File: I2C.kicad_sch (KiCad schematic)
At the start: 12 parts, among them U15 TCA9548AMRGER

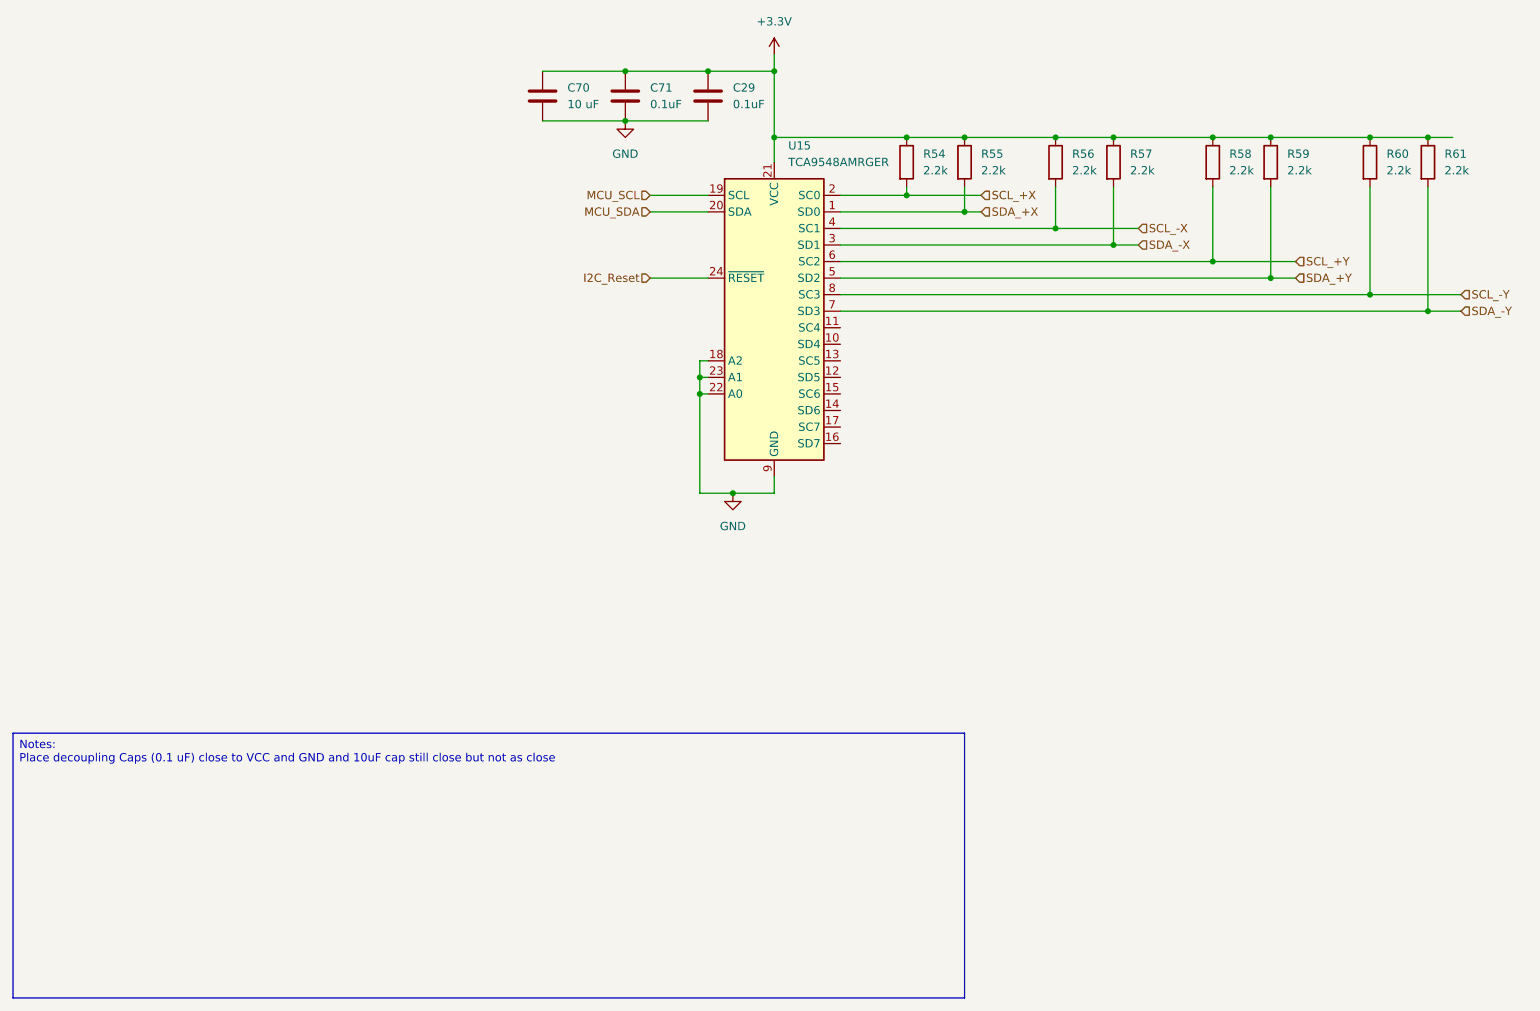
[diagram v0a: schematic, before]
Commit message: Added cap to output of lines
based on LTSpice Simulation
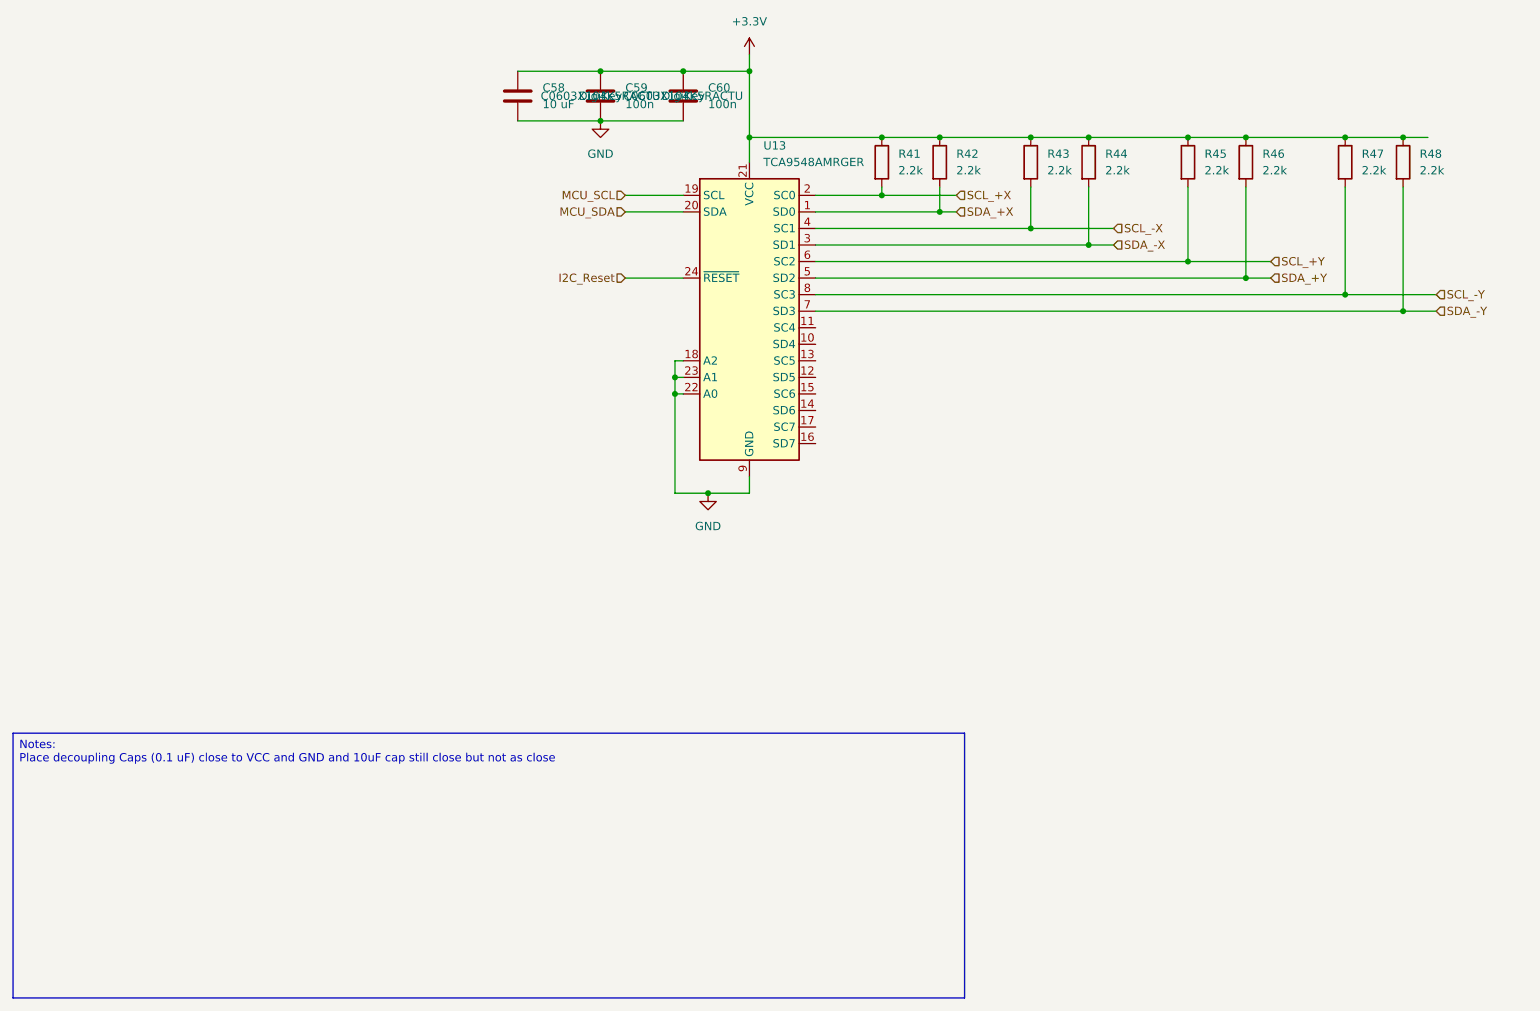
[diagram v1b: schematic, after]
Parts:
- C59: renamed from C71; value 0.1uF -> 100n; footprint (none) -> Capacitor_SMD:C_0603_1608Metric; MANUFACTURER (none) -> DigiKey; MANUFACTURER_PART_NUMBER (none) -> C0603X104K5RACTU
- C60: renamed from C29; value 0.1uF -> 100n; footprint (none) -> Capacitor_SMD:C_0603_1608Metric; MANUFACTURER (none) -> DigiKey; MANUFACTURER_PART_NUMBER (none) -> C0603X104K5RACTU
- U13: renamed from U15; footprint Package_DFN_QFN:Texas_RGE0024C_VQFN-24-1EP_4x4mm_P0.5mm_EP2.1x2.1mm -> LTC4162IUFD-LADM_PBF:QFN50P500X400X80-29N
- renumbered C70 to C58, R54 to R41, R55 to R42, R56 to R43, R57 to R44, R58 to R45, R59 to R46, R60 to R47, R61 to R48
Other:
- company: (none) -> QSET (Jaron Cyna)
- title: (none) -> I2C Multiplexer
- moved on the sheet: C58, C59, C60, R41, R42, R43, R44, R45, R46, R47, R48, U13

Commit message: Added footprints to caps
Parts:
- C55: renamed from C58; footprint (none) -> Capacitor_SMD:C_1206_3216Metric; MANUFACTURER (none) -> DigiKey; MANUFACTURER_PART_NUMBER (none) -> CL31B106KAHNFNE
- renumbered C59 to C56, C60 to C57
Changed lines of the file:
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@@
 		(dnp no)
 		(fields_autoplaced yes)
-		(property "Reference" "C59"
+		(property "Reference" "C56"
 			(at 110.49 54.6099 0)
 			(effects
@@
 					(size 1.27 1.27)
 				)
+				(hide yes)
 			)
 		)
@@
 					(size 1.27 1.27)
 				)
+				(hide yes)
 			)
 		)
@@
 			(project "EPS_mppt_board"
 				(path "/8f246f89-1ec7-4136-9977-839b50e116ed/0b35a7b5-b504-4fbf-9bb2-d6dcd13c2d56"
-					(reference "C59")
+					(reference "C56")
 					(unit 1)
 				)
@@
 		(dnp no)
 		(fields_autoplaced yes)
-		(property "Reference" "C58"
+		(property "Reference" "C55"
 			(at 97.79 54.6099 0)
 			(effects
@@
 			)
 		)
-		(property "Footprint" ""
+		(property "Footprint" "Capacitor_SMD:C_1206_3216Metric"
 			(at 94.9452 59.69 0)
 			(effects
@@
 			)
 		)
+		(property "MANUFACTURER" "DigiKey"
+			(at 93.98 55.88 0)
+			(effects
+				(font
+					(size 1.27 1.27)
+				)
+			)
+		)
+		(property "MANUFACTURER_PART_NUMBER" "CL31B106KAHNFNE"
+			(at 93.98 55.88 0)
+			(effects
+				(font
+					(size 1.27 1.27)
+				)
+			)
+		)
 		(pin "1"
 		)
@@
 			(project "EPS_mppt_board"
 				(path "/8f246f89-1ec7-4136-9977-839b50e116ed/0b35a7b5-b504-4fbf-9bb2-d6dcd13c2d56"
-					(reference "C58")
+					(reference "C55")
 					(unit 1)
 				)
@@
 		(dnp no)
 		(fields_autoplaced yes)
-		(property "Reference" "C60"
+		(property "Reference" "C57"
 			(at 123.19 54.6099 0)
 			(effects
@@
 					(size 1.27 1.27)
 				)
+				(hide yes)
 			)
 		)
@@
 					(size 1.27 1.27)
 				)
+				(hide yes)
 			)
 		)
@@
 			(project ""
 				(path "/8f246f89-1ec7-4136-9977-839b50e116ed/0b35a7b5-b504-4fbf-9bb2-d6dcd13c2d56"
-					(reference "C60")
-					(unit 1)
-				)
+					(reference "C57")
+					(unit 1)
+				)

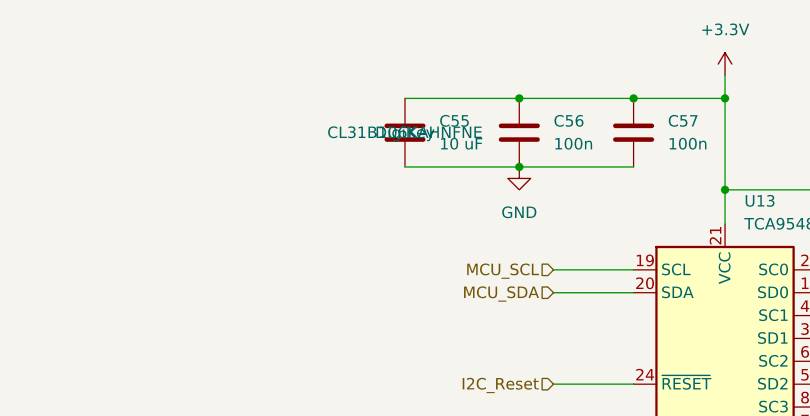
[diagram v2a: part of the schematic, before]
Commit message: edited 3V3 Logic to add Efuse and UVLO
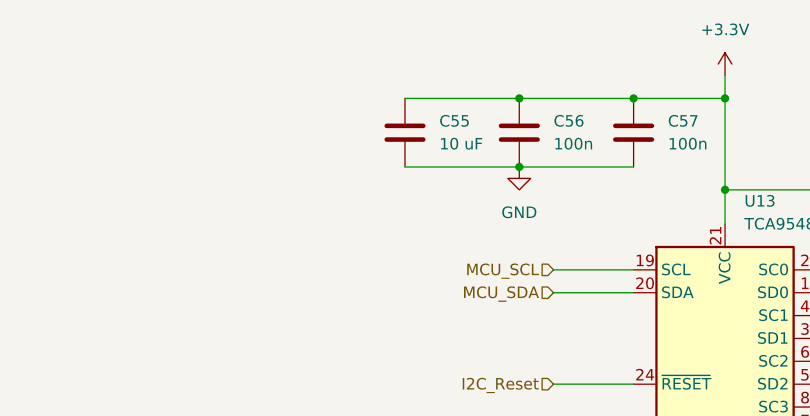
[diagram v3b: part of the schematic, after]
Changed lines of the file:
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@@
 					(size 1.27 1.27)
 				)
+				(hide yes)
 			)
 		)
@@
 					(size 1.27 1.27)
 				)
+				(hide yes)
 			)
 		)

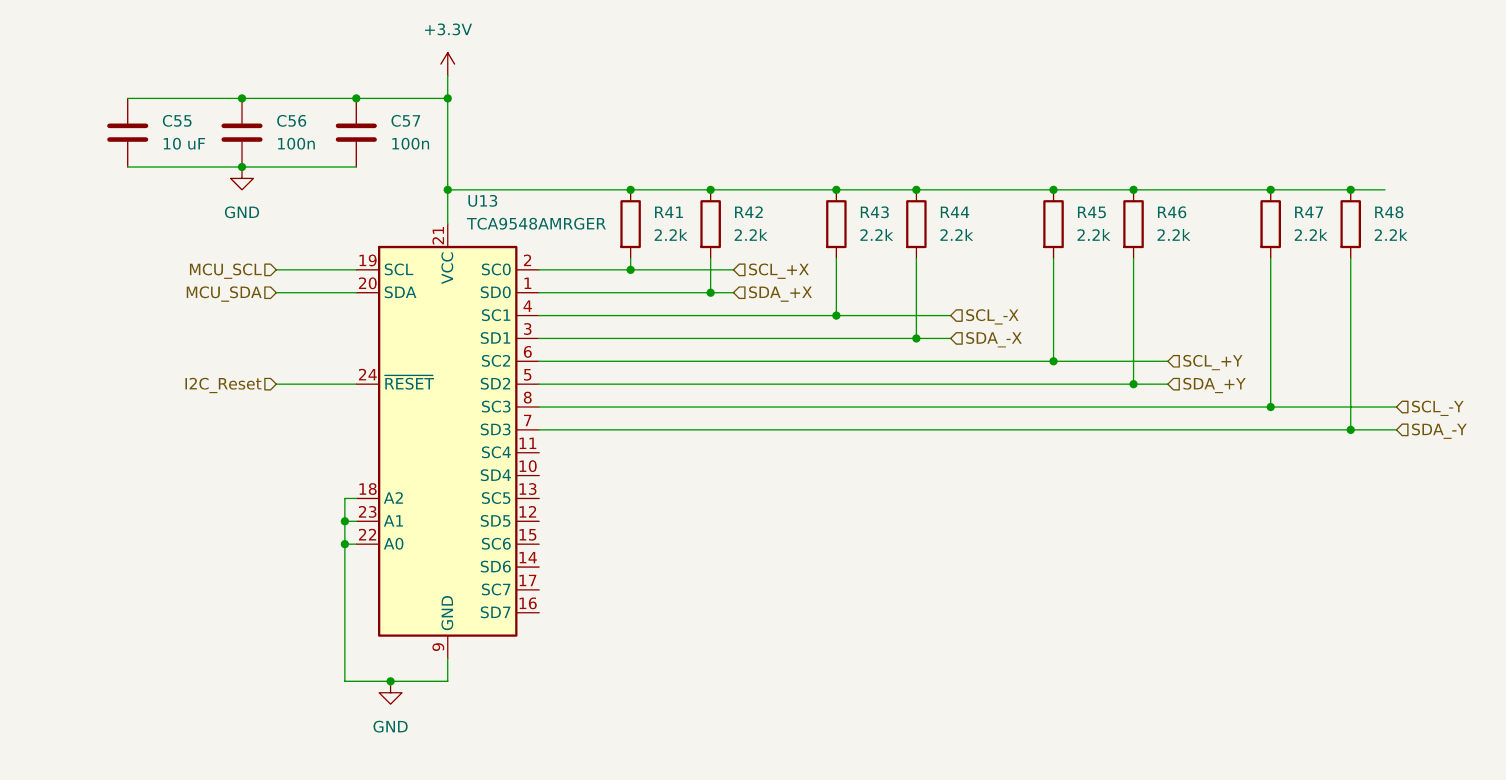
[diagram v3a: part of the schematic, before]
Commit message: Added connectors to schematic
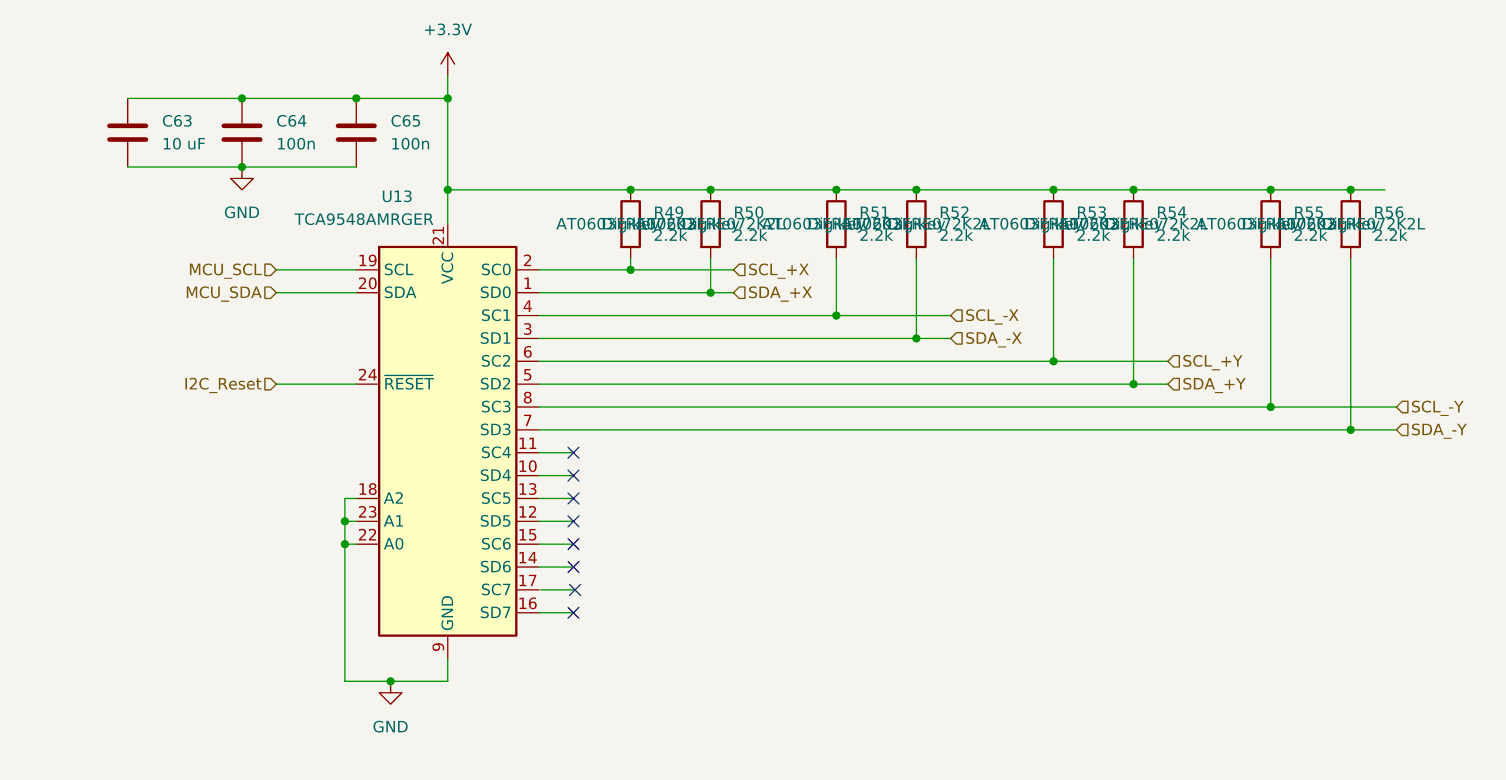
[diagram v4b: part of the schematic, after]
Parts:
- C63: renamed from C55; footprint Capacitor_SMD:C_1206_3216Metric -> zLibrary:CAP_C1210C_X7R_2S_FW_KEM-M; MANUFACTURER_PART_NUMBER CL31B106KAHNFNE -> C1210C106M5R2C7186
- R49: renamed from R41; footprint (none) -> Resistor_SMD:R_0603_1608Metric; MANUFACTURER (none) -> Digikey; MANUFACTURER_PART_NUMBER (none) -> AT0603FRE072K2L
- R50: renamed from R42; footprint (none) -> Resistor_SMD:R_0603_1608Metric; MANUFACTURER (none) -> Digikey; MANUFACTURER_PART_NUMBER (none) -> AT0603FRE072K2L
- R51: renamed from R43; footprint (none) -> Resistor_SMD:R_0603_1608Metric; MANUFACTURER (none) -> Digikey; MANUFACTURER_PART_NUMBER (none) -> AT0603FRE072K2L
- R52: renamed from R44; footprint (none) -> Resistor_SMD:R_0603_1608Metric; MANUFACTURER (none) -> Digikey; MANUFACTURER_PART_NUMBER (none) -> AT0603FRE072K2L
- R53: renamed from R45; footprint (none) -> Resistor_SMD:R_0603_1608Metric; MANUFACTURER (none) -> Digikey; MANUFACTURER_PART_NUMBER (none) -> AT0603FRE072K2L
- R54: renamed from R46; footprint (none) -> Resistor_SMD:R_0603_1608Metric; MANUFACTURER (none) -> Digikey; MANUFACTURER_PART_NUMBER (none) -> AT0603FRE072K2L
- R55: renamed from R47; footprint (none) -> Resistor_SMD:R_0603_1608Metric; MANUFACTURER (none) -> Digikey; MANUFACTURER_PART_NUMBER (none) -> AT0603FRE072K2L
- R56: renamed from R48; footprint (none) -> Resistor_SMD:R_0603_1608Metric; MANUFACTURER (none) -> Digikey; MANUFACTURER_PART_NUMBER (none) -> AT0603FRE072K2L
- U13: footprint LTC4162IUFD-LADM_PBF:QFN50P500X400X80-29N -> Package_DFN_QFN:Texas_RGE0024C_VQFN-24-1EP_4x4mm_P0.5mm_EP2.1x2.1mm
- renumbered C56 to C64, C57 to C65
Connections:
- no-connect marks 0 -> 8

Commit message: A bunch of misc schematic changes
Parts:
- renumbered C63 to C27, C64 to C28, C65 to C29, R49 to R21, R50 to R22, R51 to R23, R52 to R24, R53 to R25, R54 to R26, R55 to R27, R56 to R28, U13 to U10
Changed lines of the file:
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@@
 		(dnp no)
 		(fields_autoplaced yes)
-		(property "Reference" "R54"
+		(property "Reference" "R26"
 			(at 208.28 64.7699 0)
 			(effects
@@
 			(project "EPS_mppt_board"
 				(path "/8f246f89-1ec7-4136-9977-839b50e116ed/0b35a7b5-b504-4fbf-9bb2-d6dcd13c2d56"
-					(reference "R54")
+					(reference "R26")
 					(unit 1)
 				)
@@
 		(dnp no)
 		(fields_autoplaced yes)
-		(property "Reference" "C64"
+		(property "Reference" "C28"
 			(at 110.49 54.6099 0)
 			(effects
@@
 			(project "EPS_mppt_board"
 				(path "/8f246f89-1ec7-4136-9977-839b50e116ed/0b35a7b5-b504-4fbf-9bb2-d6dcd13c2d56"
-					(reference "C64")
+					(reference "C28")
 					(unit 1)
 				)
@@
 		(dnp no)
 		(fields_autoplaced yes)
-		(property "Reference" "C63"
+		(property "Reference" "C27"
 			(at 97.79 54.6099 0)
 			(effects
@@
 			(project "EPS_mppt_board"
 				(path "/8f246f89-1ec7-4136-9977-839b50e116ed/0b35a7b5-b504-4fbf-9bb2-d6dcd13c2d56"
-					(reference "C63")
+					(reference "C27")
 					(unit 1)
 				)
@@
 		(dnp no)
 		(fields_autoplaced yes)
-		(property "Reference" "#PWR0120"
+		(property "Reference" "#PWR057"
 			(at 123.19 123.19 0)
 			(effects
@@
 			(project ""
 				(path "/8f246f89-1ec7-4136-9977-839b50e116ed/0b35a7b5-b504-4fbf-9bb2-d6dcd13c2d56"
-					(reference "#PWR0120")
+					(reference "#PWR057")
 					(unit 1)
 				)
@@
 		(dnp no)
 		(fields_autoplaced yes)
-		(property "Reference" "R50"
+		(property "Reference" "R22"
 			(at 161.29 64.7699 0)
 			(effects
@@
 			(project "EPS_mppt_board"
 				(path "/8f246f89-1ec7-4136-9977-839b50e116ed/0b35a7b5-b504-4fbf-9bb2-d6dcd13c2d56"
-					(reference "R50")
+					(reference "R22")
 					(unit 1)
 				)
@@
 		(dnp no)
 		(fields_autoplaced yes)
-		(property "Reference" "R51"
+		(property "Reference" "R23"
 			(at 175.26 64.7699 0)
 			(effects
@@
 			(project "EPS_mppt_board"
 				(path "/8f246f89-1ec7-4136-9977-839b50e116ed/0b35a7b5-b504-4fbf-9bb2-d6dcd13c2d56"
-					(reference "R51")
+					(reference "R23")
 					(unit 1)
 				)
@@
 		(dnp no)
 		(fields_autoplaced yes)
-		(property "Reference" "#PWR0119"
+		(property "Reference" "#PWR056"
 			(at 106.68 66.04 0)
 			(effects
@@
 			(project "EPS_mppt_board"
 				(path "/8f246f89-1ec7-4136-9977-839b50e116ed/0b35a7b5-b504-4fbf-9bb2-d6dcd13c2d56"
-					(reference "#PWR0119")
+					(reference "#PWR056")
 					(unit 1)
 				)
@@
 		(dnp no)
 		(fields_autoplaced yes)
-		(property "Reference" "R49"
+		(property "Reference" "R21"
 			(at 152.4 64.7699 0)
 			(effects
@@
 			(project ""
 				(path "/8f246f89-1ec7-4136-9977-839b50e116ed/0b35a7b5-b504-4fbf-9bb2-d6dcd13c2d56"
-					(reference "R49")
+					(reference "R21")
 					(unit 1)
 				)
@@
 		(dnp no)
 		(fields_autoplaced yes)
-		(property "Reference" "R52"
+		(property "Reference" "R24"
 			(at 184.15 64.7699 0)
 			(effects
@@
 			(project "EPS_mppt_board"
 				(path "/8f246f89-1ec7-4136-9977-839b50e116ed/0b35a7b5-b504-4fbf-9bb2-d6dcd13c2d56"
-					(reference "R52")
+					(reference "R24")
 					(unit 1)
 				)
@@
 		(on_board yes)
 		(dnp no)
-		(property "Reference" "U13"
+		(property "Reference" "U10"
 			(at 122.174 62.992 0)
 			(effects
@@
 			(project ""
 				(path "/8f246f89-1ec7-4136-9977-839b50e116ed/0b35a7b5-b504-4fbf-9bb2-d6dcd13c2d56"
-					(reference "U13")
+					(reference "U10")
 					(unit 1)
 				)
@@
 		(dnp no)
 		(fields_autoplaced yes)
-		(property "Reference" "R55"
+		(property "Reference" "R27"
 			(at 223.52 64.7699 0)
 			(effects
@@
 			(project "EPS_mppt_board"
 				(path "/8f246f89-1ec7-4136-9977-839b50e116ed/0b35a7b5-b504-4fbf-9bb2-d6dcd13c2d56"
-					(reference "R55")
+					(reference "R27")
 					(unit 1)
 				)
@@
 		(dnp no)
 		(fields_autoplaced yes)
-		(property "Reference" "R56"
+		(property "Reference" "R28"
 			(at 232.41 64.7699 0)
 			(effects
@@
 			(project "EPS_mppt_board"
 				(path "/8f246f89-1ec7-4136-9977-839b50e116ed/0b35a7b5-b504-4fbf-9bb2-d6dcd13c2d56"
-					(reference "R56")
+					(reference "R28")
 					(unit 1)
 				)
@@
 		(dnp no)
 		(fields_autoplaced yes)
-		(property "Reference" "C65"
+		(property "Reference" "C29"
 			(at 123.19 54.6099 0)
 			(effects
@@
 			(project ""
 				(path "/8f246f89-1ec7-4136-9977-839b50e116ed/0b35a7b5-b504-4fbf-9bb2-d6dcd13c2d56"
-					(reference "C65")
+					(reference "C29")
 					(unit 1)
 				)
@@
 		(dnp no)
 		(fields_autoplaced yes)
-		(property "Reference" "#PWR0118"
+		(property "Reference" "#PWR055"
 			(at 129.54 53.34 0)
 			(effects
@@
 			(project ""
 				(path "/8f246f89-1ec7-4136-9977-839b50e116ed/0b35a7b5-b504-4fbf-9bb2-d6dcd13c2d56"
-					(reference "#PWR0118")
+					(reference "#PWR055")
 					(unit 1)
 				)
@@
 		(dnp no)
 		(fields_autoplaced yes)
-		(property "Reference" "R53"
+		(property "Reference" "R25"
 			(at 199.39 64.7699 0)
 			(effects
@@
 			(project "EPS_mppt_board"
 				(path "/8f246f89-1ec7-4136-9977-839b50e116ed/0b35a7b5-b504-4fbf-9bb2-d6dcd13c2d56"
-					(reference "R53")
-					(unit 1)
-				)
+					(reference "R25")
+					(unit 1)
+				)
